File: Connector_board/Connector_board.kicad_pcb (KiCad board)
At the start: 2 copper layers, 54.2 x 20 mm, 7 parts, among them J1 USB_B_Micro, J2 Conn_02x04_Counter_Clockwise, J3 Conn_02x06_Counter_Clockwise, J4 Conn_02x07_Counter_Clockwise, J5 SM03B-SRSS-TB

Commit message: test PCB version 2 completed
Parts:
- removed the J2 at (35.1, 42.6)
- added J4: Conn_02x07_Odd_Even, Connector_PinHeader_2.54mm:PinHeader_2x07_P2.54mm_Vertical, F.Cu at (46.5, 35.7)
- J3: value Conn_02x06_Counter_Clockwise -> Conn_02x07_Counter_Clockwise; footprint Connector_PinHeader_2.54mm:PinHeader_2x06_P2.54mm_Vertical -> Connector_Molex:Molex_SlimStack_502430-1410_2x07_P0.40mm_Vertical
- moved J3 14.6 mm to (35.5, 42.7), turned to -90 degrees
- renumbered J5 to J1, J1 to J2, J4 to J5
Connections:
- J2 pad 1: +3V3 -> +5V
- J3 pad 1: GND -> /SWD_1
- J3 pad 11: /POSITION_OUT_1 -> unconnected-(J3-Pin_11-Pad11)
- J3 pad 2: unconnected-(J3-Pin_2-Pad2) -> +5V
- J3 pad 3: /IMAGE_OUT_1_1+ -> /SWCLK_1
- J3 pad 5: /IMAGE_OUT_2_1+ -> /USB_D1-
- J3 pad 7: /IMAGE_OUT_2_1- -> /USB_D1+
- J3 pad 9: /IMAGE_OUT_1_1- -> unconnected-(J3-Pin_9-Pad9)
- J5 pad 1: /IMAGE_OUT_1_1+ -> /HREF_OUT
- J5 pad 11: GND -> /IMAGE_OUT_1
- J5 pad 13: unconnected-(J4-Pin_13-Pad13) -> /FPGA_EN
- J5 pad 14: unconnected-(J4-Pin_14-Pad14) -> GND
- J5 pad 3: /IMAGE_OUT_2_1+ -> /POSITION_OUT_1
- J5 pad 4: unconnected-(J4-Pin_4-Pad4) -> /IMAGE_CLK
- J5 pad 5: /IMAGE_OUT_2_1- -> /IMAGE_OUT_4
- J5 pad 6: unconnected-(J4-Pin_6-Pad6) -> /VSYNC_OUT
- J5 pad 7: /IMAGE_OUT_1_1- -> /IMAGE_OUT_3
- J5 pad 8: unconnected-(J4-Pin_8-Pad8) -> /POSITION_OUT_CLK
- J5 pad 9: /POSITION_OUT_1 -> /IMAGE_OUT_2
- R1 pad 1: +3V3 -> +5V
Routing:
- net /HREF_OUT: track 0.00 -> 28.2 mm, vias 0 -> 1
- net /FPGA_EN: track 0.00 -> 25.8 mm, vias 0 -> 1
- net /IMAGE_OUT_4: track 0.00 -> 24.9 mm, vias 0 -> 1
- net /IMAGE_OUT_1: track 0.00 -> 24.2 mm, vias 0 -> 1
- net /IMAGE_OUT_3: track 0.00 -> 24.2 mm, vias 0 -> 1
- net /IMAGE_OUT_2: track 0.00 -> 23.7 mm, vias 0 -> 1
- net /IMAGE_OUT_2_1-: track 20.7 -> 0.00 mm, vias 1 -> 0
- net /IMAGE_OUT_2_1+: track 20.5 -> 0.00 mm, vias 1 -> 0
- net /IMAGE_OUT_1_1+: track 19.9 -> 0.00 mm, vias 1 -> 0
- net /IMAGE_OUT_1_1-: track 19.9 -> 0.00 mm, vias 1 -> 0
- net /IMAGE_CLK: track 0.00 -> 16.3 mm
- net /VSYNC_OUT: track 0.00 -> 15.5 mm
- net /POSITION_OUT_CLK: track 0.00 -> 14.6 mm
- net +5V: track 0.00 -> 14.5 mm
- net /POSITION_OUT_1: track 20.8 -> 25.9 mm
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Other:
- board text added: "5V"
- board text added: "FPGA_EN"
- board text added: "GND"
- board text added: "HREF"
- board text added: "IMG_CLK"
- board text added: "IMG_OUT1"
- board text added: "IMG_OUT2"
- board text added: "IMG_OUT3"
- board text added: "IMG_OUT4"
- board text added: "PO_CLK"
- board text added: "PO_OUT1"
- board text added: "VSYNC_OUT"
- board text removed: "IO1+"
- board text removed: "IO1-"
- board text removed: "IO2+"
- board text removed: "IO2-"
- board text removed: "PO"

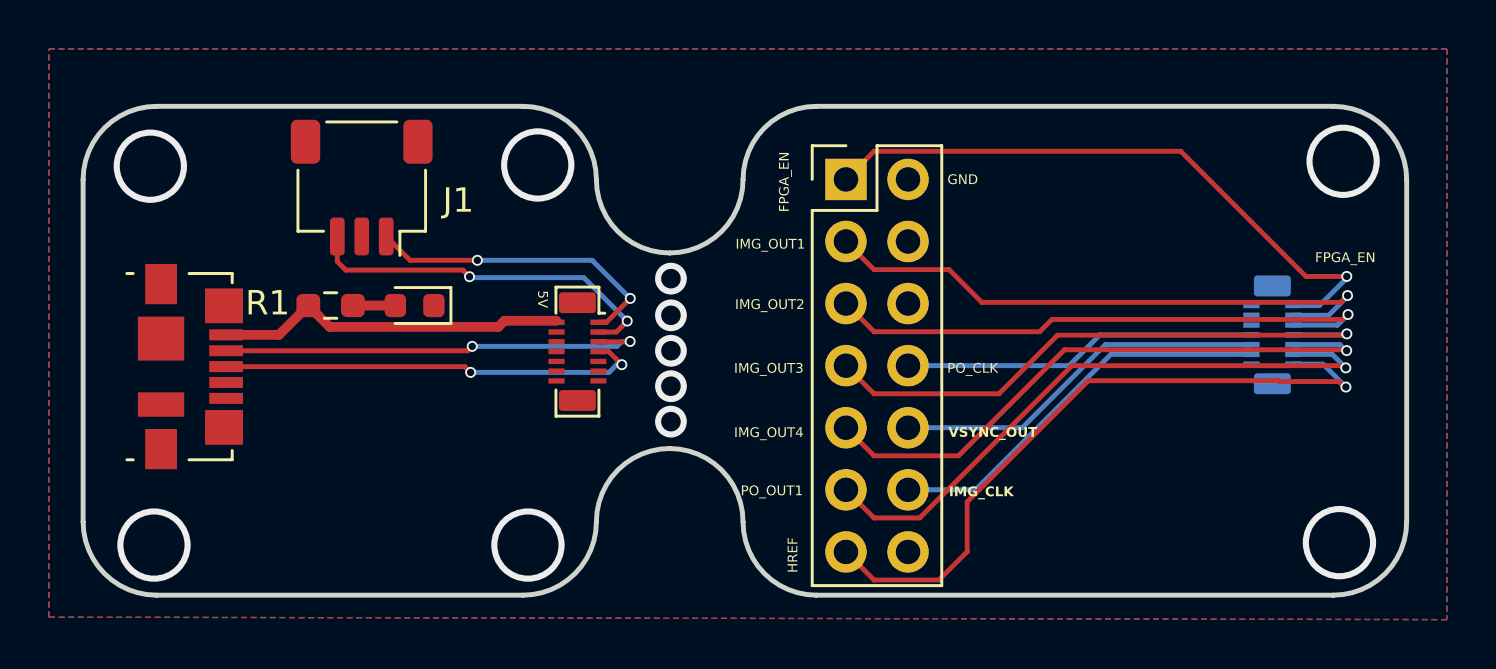
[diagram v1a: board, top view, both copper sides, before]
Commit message: refined 5V net isolation
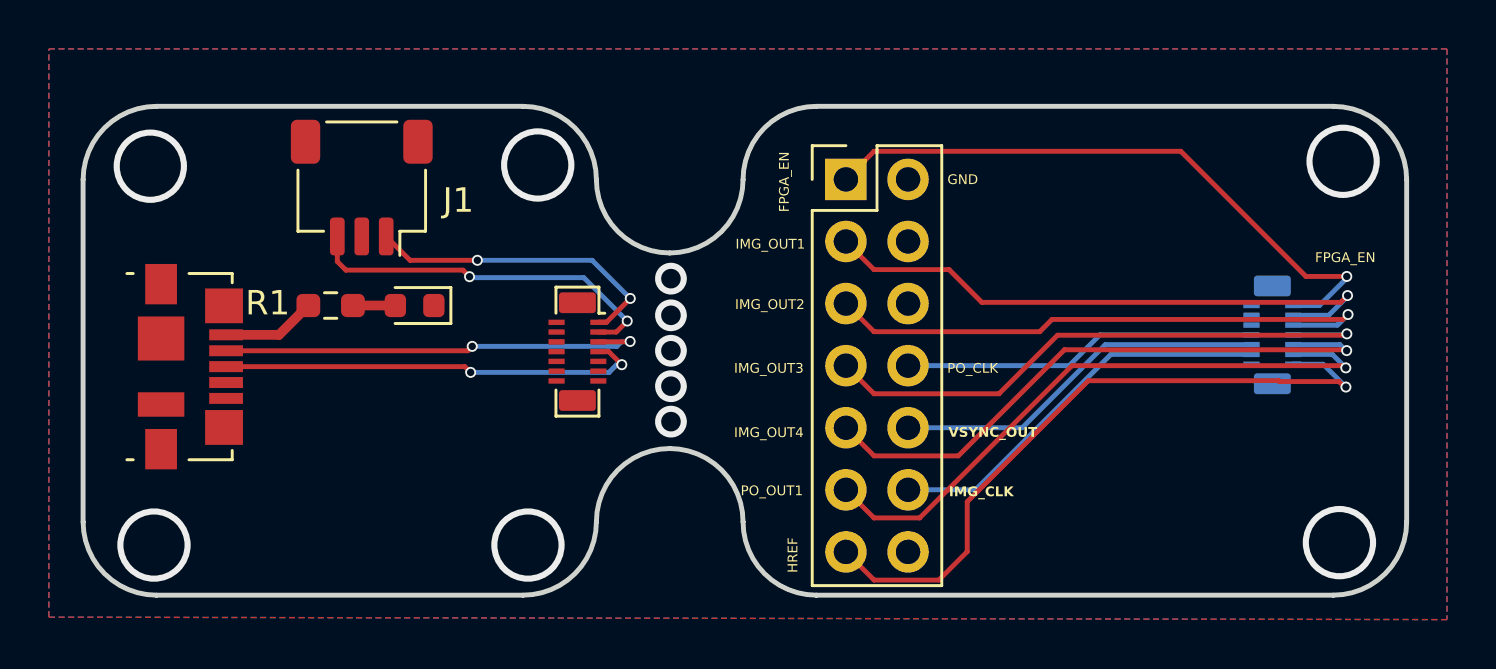
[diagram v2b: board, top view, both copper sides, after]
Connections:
- J3 pad 2: +5V -> unconnected-(J3-Pin_2-Pad2)
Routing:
- net +5V: track 14.5 -> 3.86 mm
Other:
- board text removed: "5V"
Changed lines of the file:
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@@
 		(sheetname "/")
 		(sheetfile "Connector_board.kicad_sch")
+		(units
+			(unit
+				(name "A")
+				(pins "1" "3" "5" "7" "9" "11" "13" "2" "4" "6" "8" "10" "12" "14")
+			)
+		)
 		(clearance 0.15)
 		(attr smd)
@@
 			(size 0.22 0.66)
 			(layers "F.Cu" "F.Mask" "F.Paste")
-			(net "+5V")
+			(net "unconnected-(J3-Pin_2-Pad2)")
 			(pinfunction "Pin_2_2")
-			(pintype "passive")
+			(pintype "passive+no_connect")
 		)
 		(pad "3" smd rect
@@
 		(sheetname "/")
 		(sheetfile "Connector_board.kicad_sch")
+		(units
+			(unit
+				(name "A")
+				(pins "1" "3" "5" "7" "9" "11" "13" "2" "4" "6" "8" "10" "12" "14")
+			)
+		)
 		(clearance 0.15)
 		(attr smd)
@@
 		)
 		(pad "15" smd roundrect
-			(at -2 0 180)
+			(at -2 0)
 			(size 1.509998 0.8508)
 			(layers "B.Cu" "B.Mask" "B.Paste")
@@
 		)
 		(pad "15" smd roundrect
-			(at 2 0 180)
+			(at 2 0)
 			(size 1.509998 0.8508)
 			(layers "B.Cu" "B.Mask" "B.Paste")
@@
 		)
 	)
-	(gr_text "5V"
-		(at 33.87 40.23 270)
-		(layer "F.SilkS")
-		(effects
-			(font
-				(size 0.4 0.4)
-				(thickness 0.1)
-			)
-			(justify left bottom)
-		)
-	)
 	(segment
 		(start 28.675 39)
@@
 		(width 0.4)
 		(layer "F.Cu")
-		(net "+5V")
-	)
-	(segment
-		(start 32.285 41.725)
-		(end 32.535 41.475)
-		(width 0.4)
-		(layer "F.Cu")
-		(net "+5V")
-	)
-	(segment
-		(start 25.39 41.725)
-		(end 32.285 41.725)
-		(width 0.4)
-		(layer "F.Cu")
-		(net "+5V")
-	)
-	(segment
-		(start 32.535 41.475)
-		(end 34.67 41.475)
-		(width 0.4)
-		(layer "F.Cu")
-		(net "+5V")
-	)
-	(segment
-		(start 24.515 40.85)
-		(end 25.39 41.725)
-		(width 0.4)
-		(layer "F.Cu")
